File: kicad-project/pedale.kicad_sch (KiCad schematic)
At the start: 44 parts, among them IC1 TLV76150DCYR, IC2 TLV76150DCYR, IC3 TLV76150DCYR, IC4 TLV76150DCYR, IC5 TLV76150DCYR

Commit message: modificari 4
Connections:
- net 12V: now also J13.15 (VBAT); no longer J13.16 (VBAT)
- net GND: now also J1.12 (GND); no longer J1.11 (GND)
- net at J14.1 (ptd1): now also R0.1, R2.2
- net at R12.1, R14.2: now also J14.9 (pta9); no longer J14.10 (pta9)
- net at J14.3 (ptd0): now also R3.1, R5.2
- net at J14.5 (pta13): now also R6.1, R8.2
- net at J14.7 (pta8): now also R11.2, R9.1
- now unconnected: J14.2 (ptd1), J14.4 (ptd0), J14.6 (pta13), J14.8 (pta8)
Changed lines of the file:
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@@
 	(symbol
 		(lib_id "pedale-lib:Conn_J15")
-		(at 241.3 101.6 0)
+		(at 234.95 100.33 0)
 		(unit 1)
 		(exclude_from_sim no)
@@
 		(dnp no)
 		(property "Reference" "J1"
-			(at 234.188 85.09 0)
+			(at 227.838 83.82 0)
 			(effects
 				(font
@@
 		)
 		(property "Value" "~"
-			(at 234.315 83.82 0)
+			(at 227.965 82.55 0)
 			(effects
 				(font
@@
 		)
 		(property "Footprint" "Connector_PinHeader_2.54mm:PinHeader_2x10_P2.54mm_Vertical"
-			(at 241.3 101.6 0)
+			(at 234.95 100.33 0)
 			(effects
 				(font
@@
 		)
 		(property "Datasheet" ""
-			(at 241.3 101.6 0)
+			(at 234.95 100.33 0)
 			(effects
 				(font
@@
 		)
 		(property "Description" ""
-			(at 241.3 101.6 0)
+			(at 234.95 100.33 0)
 			(effects
 				(font

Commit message: viorel checked
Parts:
- added D1: SS32, Diode_SMD:D_SMB, symbol Diode:SS32
- added H1, H2, H3, H4, H5, H6, H7, H8: MountingHole_Pad, MountingHole:MountingHole_3.2mm_M3_DIN965_Pad, symbol Mechanical:MountingHole_Pad
- U1, U8: footprint Connector_PinSocket_2.00mm:PinSocket_1x02_P2.00mm_Horizontal -> Connector_JST:JST_PH_B2B-PH-K_1x02_P2.00mm_Vertical
- U2, U3, U5, U6, U7: footprint Connector_PinSocket_2.00mm:PinSocket_1x03_P2.00mm_Horizontal -> Connector_JST:JST_PH_B3B-PH-K_1x03_P2.00mm_Vertical
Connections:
- net 12V: now also D1.1 (K)
- net GND: now also D1.2 (A), H1.1, H2.1, H3.1, H4.1, H5.1, H6.1, H7.1, H8.1

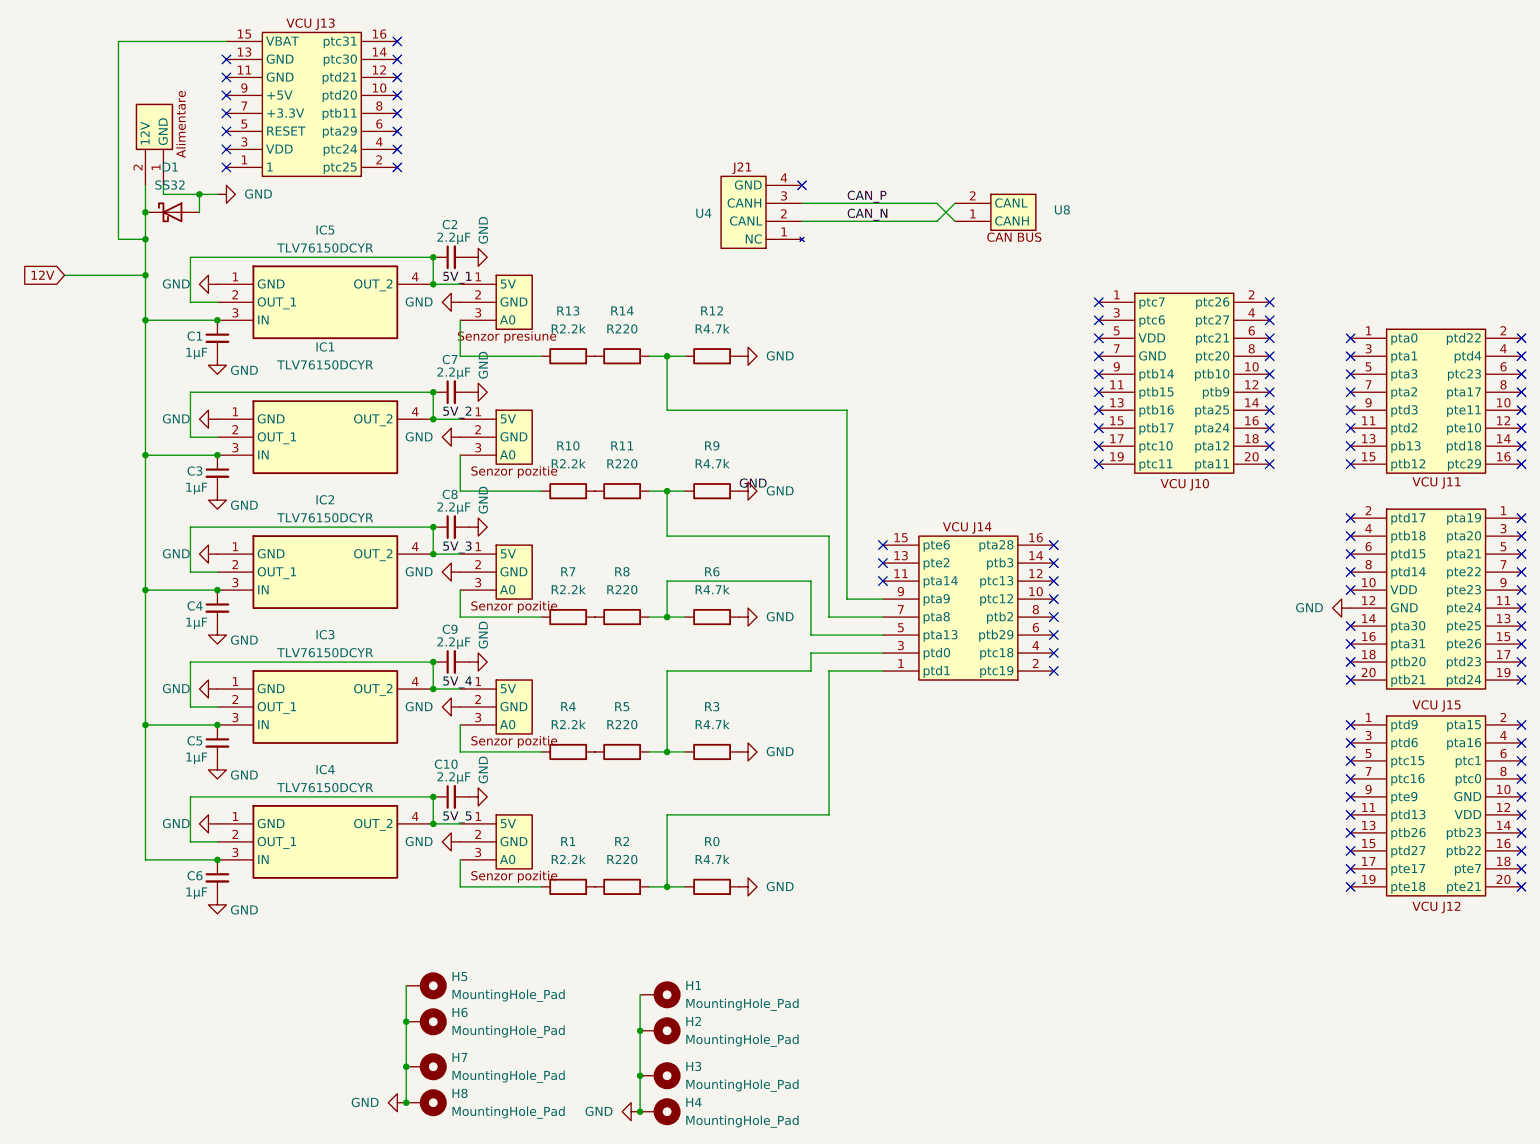
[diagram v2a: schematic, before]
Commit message: CAN_IN + CAN_OUT - added
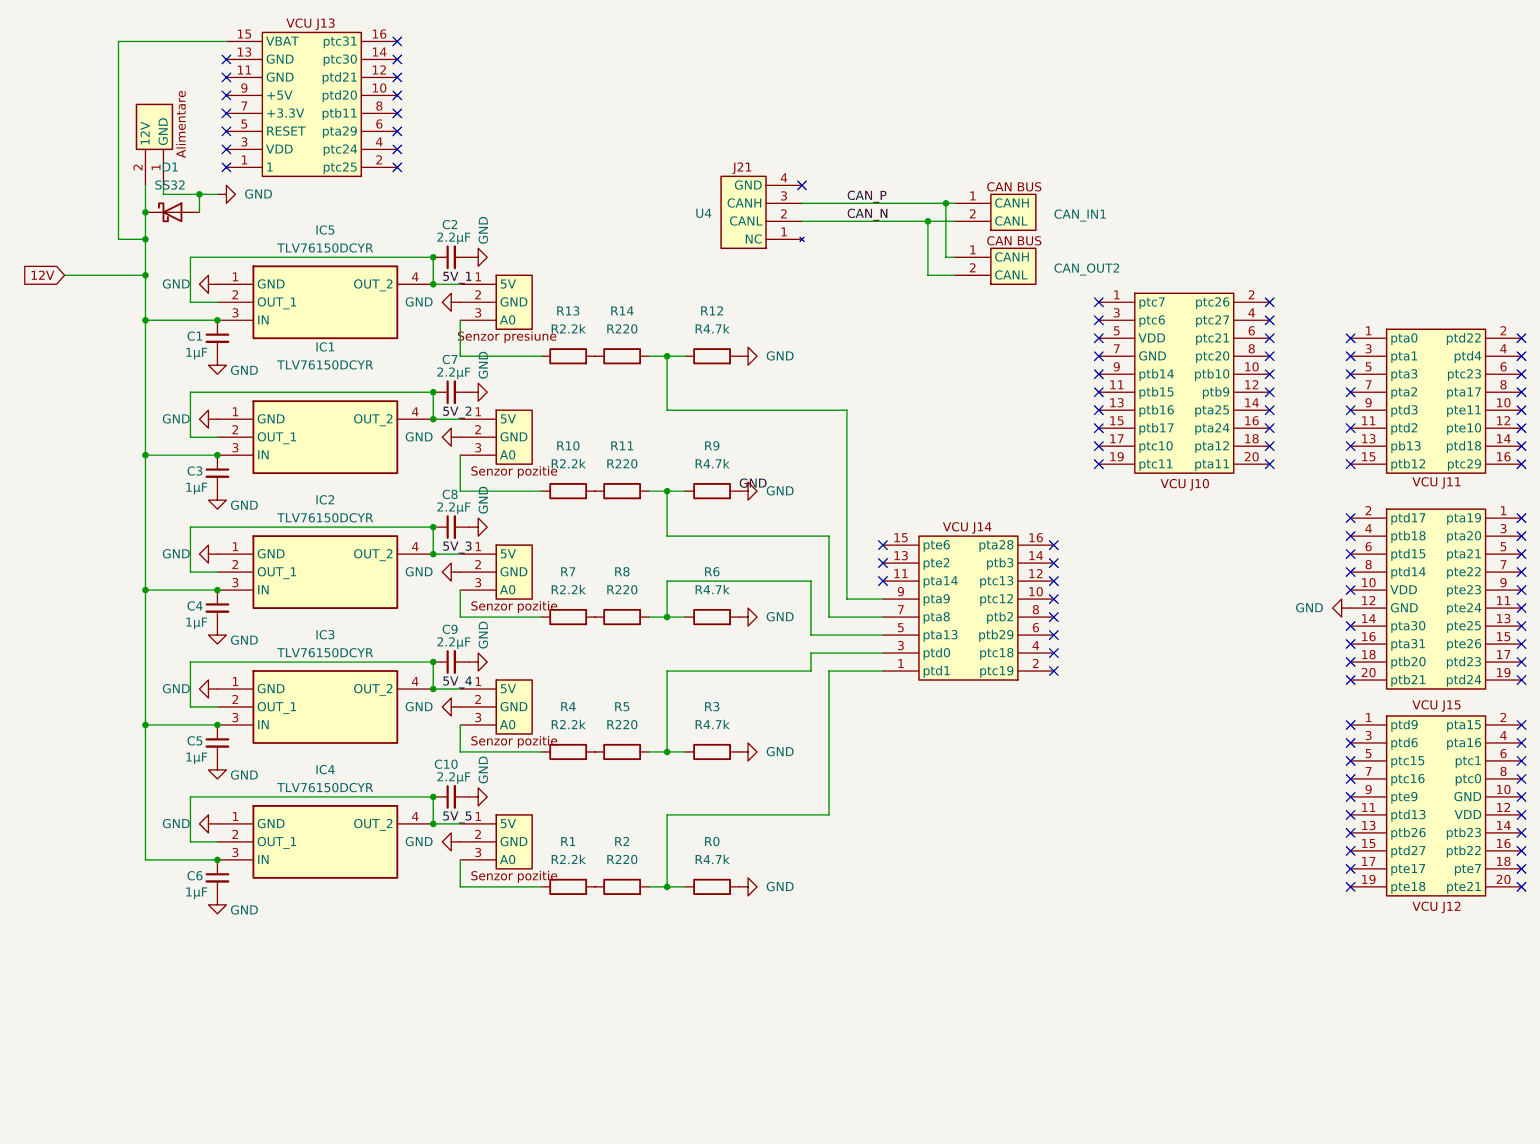
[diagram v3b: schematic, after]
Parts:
- removed H1, H2, H3, H4, H5, H6, H7, H8: MountingHole_Pad, MountingHole:MountingHole_3.2mm_M3_DIN965_Pad, symbol Mechanical:MountingHole_Pad
- added CAN_OUT2: (no value), Connector_JST:JST_PH_B2B-PH-K_1x02_P2.00mm_Vertical, symbol pedale-lib:Conn_CAN
- CAN_IN1: renamed from U8; value ~ -> (none)
- J1, J13, J14, J2, J3, J4, U1, U2, U3, U4, U5, U6, U7: value ~ -> (none)
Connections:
- net CAN_N: now also CAN_OUT2.2 (CANL)
- net CAN_P: now also CAN_OUT2.1 (CANH)
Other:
- moved on the sheet: CAN_IN1

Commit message: V_divirders removed+ Connectors moved
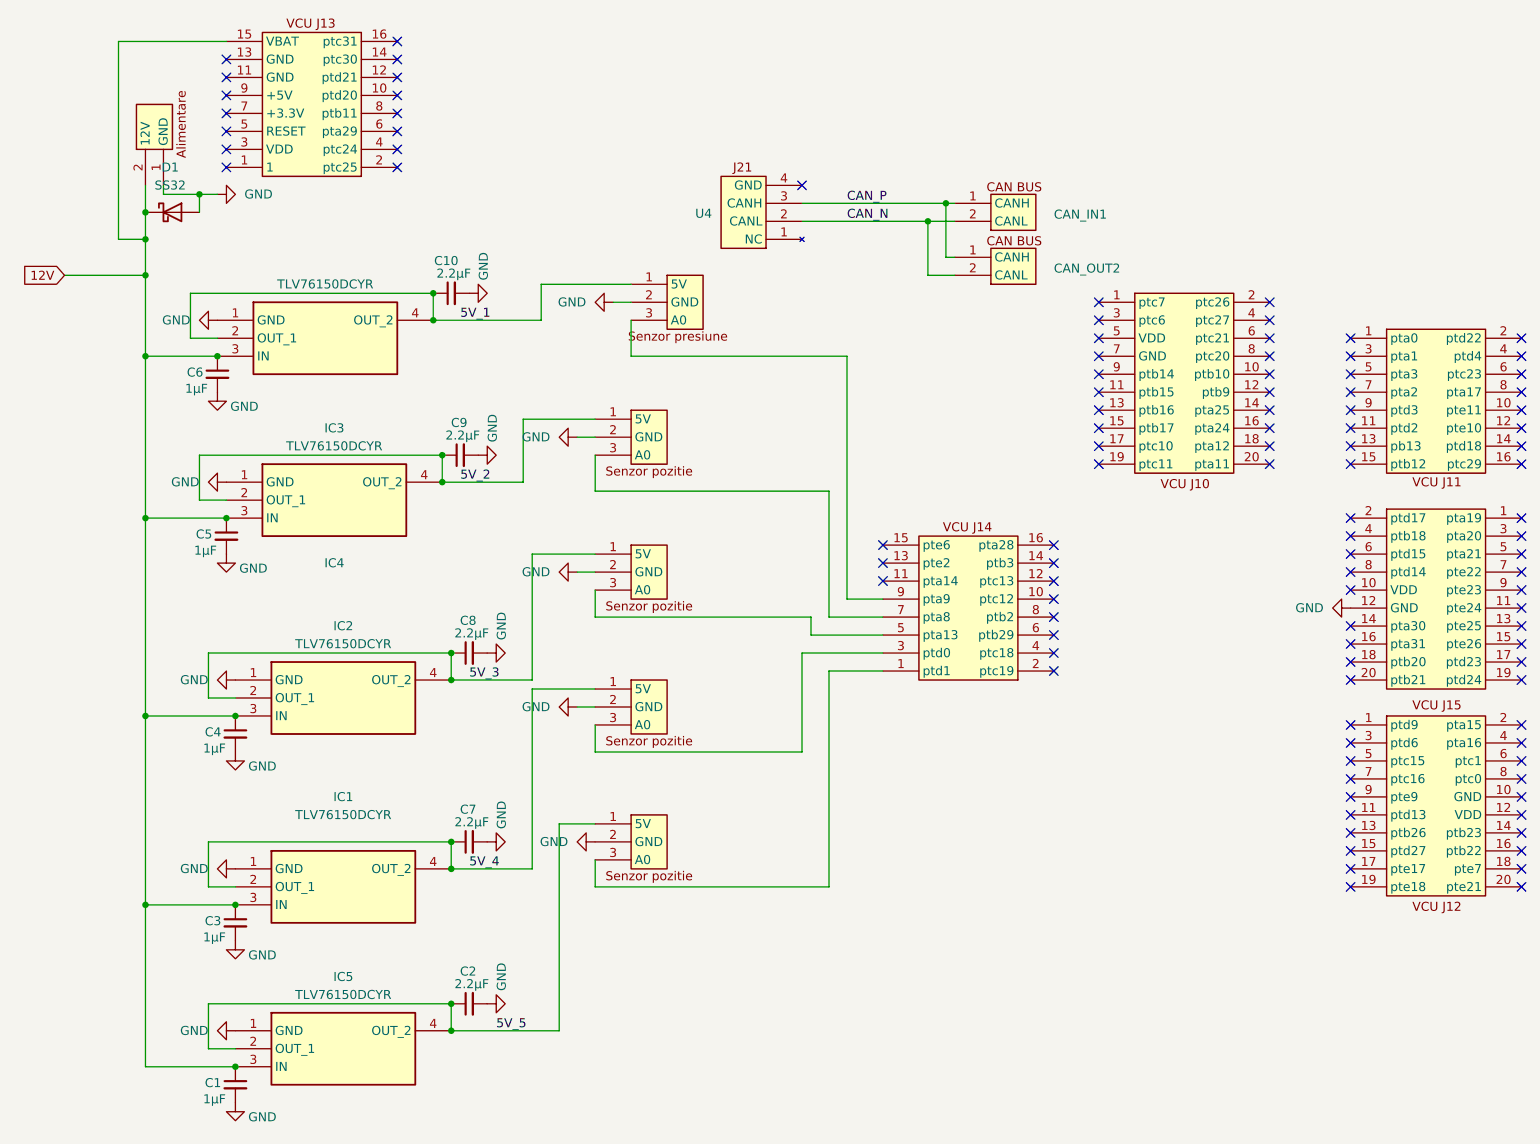
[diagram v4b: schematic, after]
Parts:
- removed R0, R12, R3, R6, R9: R4.7k, Resistor_SMD:R_2010_5025Metric_Pad1.40x2.65mm_HandSolder, symbol Device:R
- removed R1, R10, R13, R4, R7: R2.2k, Resistor_SMD:R_2010_5025Metric_Pad1.40x2.65mm_HandSolder, symbol Device:R
- removed R11, R14, R2, R5, R8: R220, Resistor_SMD:R_2010_5025Metric_Pad1.40x2.65mm_HandSolder, symbol Device:R
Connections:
- net 5V_1: now also C10.1, IC4.2 (OUT_1), IC4.4 (OUT_2); no longer C2.1, IC5.2 (OUT_1), IC5.4 (OUT_2)
- net 5V_2: now also C9.1, IC3.2 (OUT_1), IC3.4 (OUT_2); no longer C7.1, IC1.2 (OUT_1), IC1.4 (OUT_2)
- net 5V_4: now also C7.1, IC1.2 (OUT_1), IC1.4 (OUT_2); no longer C9.1, IC3.2 (OUT_1), IC3.4 (OUT_2)
- net 5V_5: now also C2.1, IC5.2 (OUT_1), IC5.4 (OUT_2); no longer C10.1, IC4.2 (OUT_1), IC4.4 (OUT_2)
- net at U3.3 (A0): now also J14.9 (pta9)
- net at J14.1 (ptd1): now also U7.3 (A0)
- net at J14.3 (ptd0): now also U6.3 (A0)
- net at J14.5 (pta13): now also U5.3 (A0)
- net at J14.7 (pta8): now also U2.3 (A0)
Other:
- moved on the sheet: C1, C10, C2, C3, C4, C5, C6, C7, C8, C9, IC1, IC2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
